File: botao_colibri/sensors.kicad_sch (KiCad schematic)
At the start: 4 parts

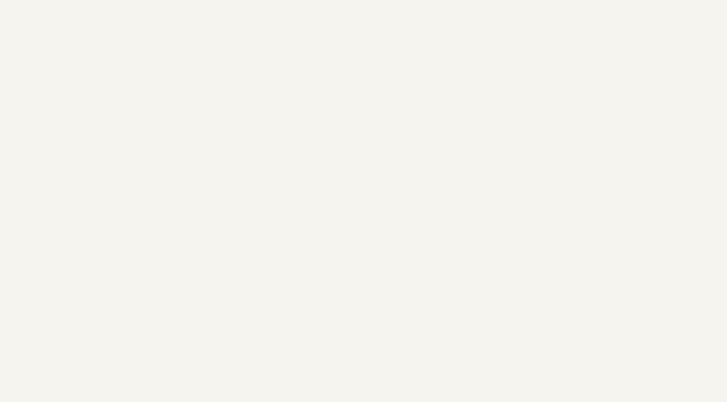
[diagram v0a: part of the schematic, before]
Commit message: chore: Update PCB/schematic edits and project files
Marks hole positions on the board, syncs KiCad project/prl files after
enabling the colibri-v4 library, and adds the botao_colibri KiCad
project files plus recent backup snapshots.

Co-Authored-By: Claude Sonnet 5 <noreply@anthropic.com>
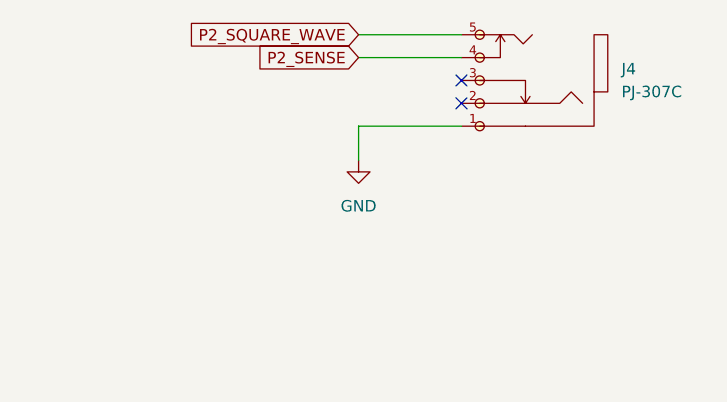
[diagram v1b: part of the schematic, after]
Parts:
- added J4: PJ-307C, botao_colibri:AUDIO-TH_PJ307C, symbol botao_colibri:PJ-307C
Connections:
- new net GND: J4.1
- new net P2_SENSE: J4.4
- new net P2_SQUARE_WAVE: J4.5
- no-connect marks 0 -> 2
